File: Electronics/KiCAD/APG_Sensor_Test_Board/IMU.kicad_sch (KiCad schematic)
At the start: 6 parts, among them U2 BNO085

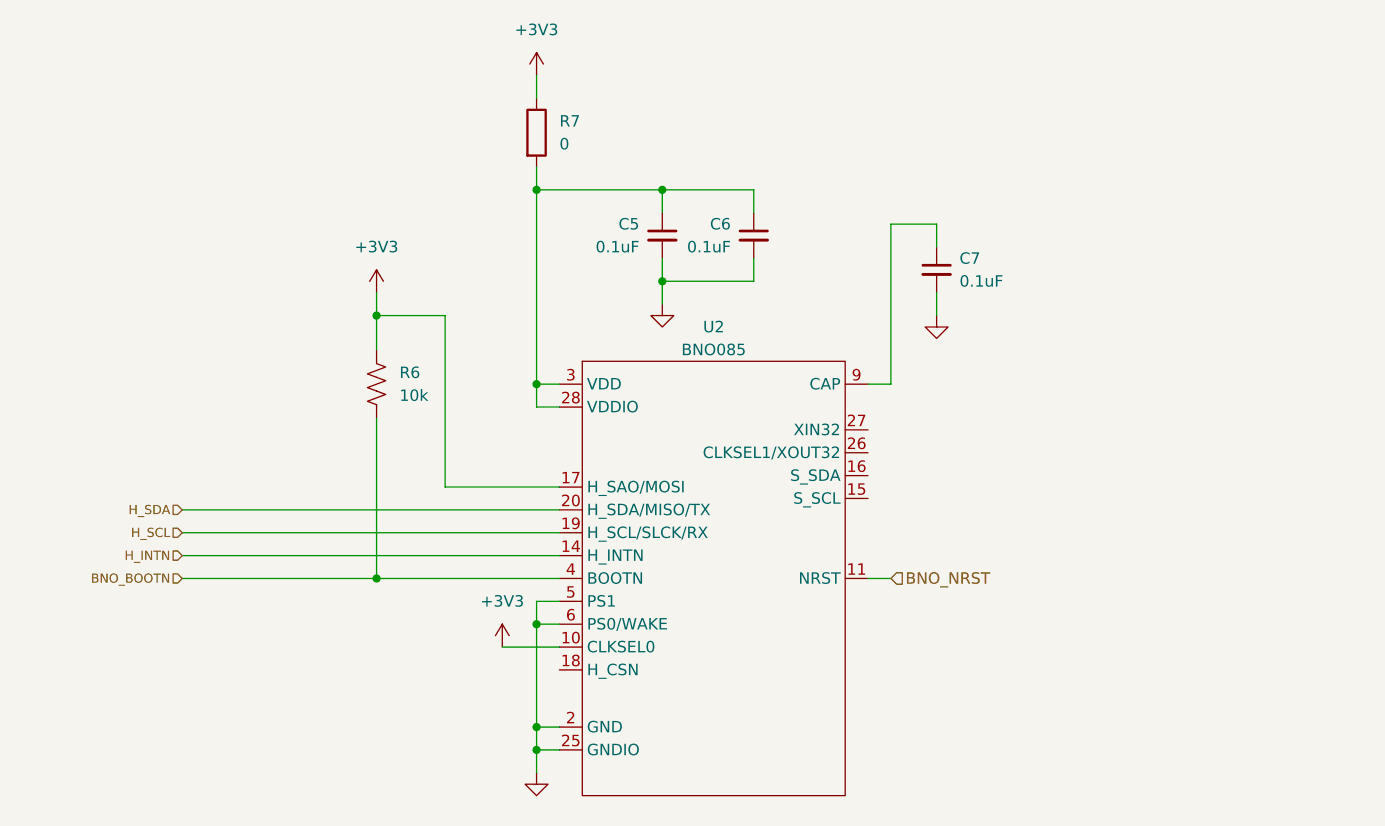
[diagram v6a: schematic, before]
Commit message: MOved IMU and HIGH G to SPI other misc changes
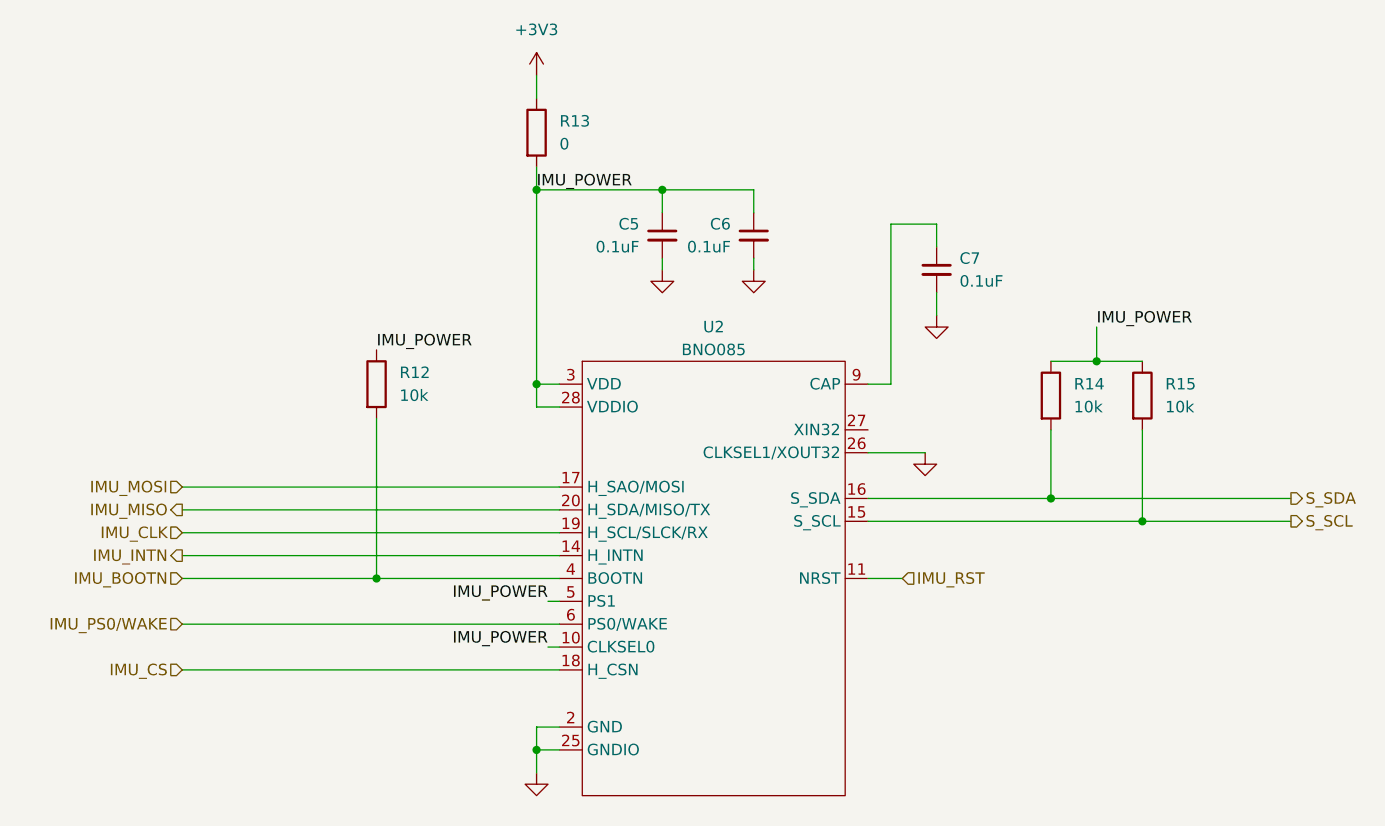
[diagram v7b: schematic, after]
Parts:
- removed R6: 10k, Resistor_SMD:R_0805_2012Metric, symbol Device:R_US
- added R12, R14, R15: 10k, Resistor_SMD:R_0805_2012Metric, symbol Device:R
- renumbered R7 to R13
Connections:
- net +3V3: no longer U2.10 (CLKSEL0), U2.17 (H_SAO/MOSI)
- net GND: now also U2.26 (CLKSEL1/XOUT32); no longer U2.5 (PS1), U2.6 (PS0/WAKE)
- net IMU_POWER: now reaches C5.1, C6.1, R13.2, U2.28 (VDDIO), U2.3 (VDD)
- net IMU_POWER: now also U2.10 (CLKSEL0), U2.5 (PS1), R12.1, R14.1, R15.1
- net S_SCL: now reaches U2.15 (S_SCL)
- net S_SCL: now also R15.2
- net S_SDA: now reaches U2.16 (S_SDA)
- net S_SDA: now also R14.2
- net IMU_CS: now reaches U2.18 (H_CSN)
- net BNO_BOOTN renamed IMU_BOOTN
- net IMU_BOOTN: now also R12.2
- net BNO_NRST renamed IMU_RST
- net H_INTN renamed IMU_INTN
- net H_SCL renamed IMU_CLK
- net H_SDA renamed IMU_MISO
- new net IMU_MOSI: U2.17 (H_SAO/MOSI)
- new net IMU_PS0/WAKE: U2.6 (PS0/WAKE)

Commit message: Layout and routing
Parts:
- added R29: 10k, Resistor_SMD:R_0603_1608Metric, symbol Device:R
- C5, C6, C7: footprint Capacitor_SMD:C_0805_2012Metric -> Capacitor_SMD:C_0603_1608Metric
- R12, R13, R14, R15: footprint Resistor_SMD:R_0805_2012Metric -> Resistor_SMD:R_0603_1608Metric
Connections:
- net IMU_CS: now also R29.2
- net IMU_POWER: now also R29.1
- net IMU_BOOTN: no longer names the net of R12.2, U2.4 (BOOTN)
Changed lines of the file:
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@@
+	)
+	(junction
+		(at 87.63 92.71)
+		(diameter 0)
+		(color 0 0 0 0)
 	)
 	(junction
@@
 	)
 	(junction
-		(at 102.87 82.55)
-		(diameter 0)
-		(color 0 0 0 0)
-	)
-	(junction
 		(at 134.62 39.37)
 		(diameter 0)
@@
 	(wire
 		(pts
+			(xy 87.63 64.77) (xy 87.63 92.71)
+		)
+		(stroke
+			(width 0)
+			(type default)
+		)
+	)
+	(wire
+		(pts
 			(xy 123.19 60.96) (xy 120.65 60.96)
 		)
@@
 	(wire
 		(pts
-			(xy 81.28 92.71) (xy 123.19 92.71)
+			(xy 81.28 92.71) (xy 87.63 92.71)
 		)
 		(stroke
@@
 	(wire
 		(pts
-			(xy 81.28 82.55) (xy 102.87 82.55)
+			(xy 87.63 92.71) (xy 123.19 92.71)
 		)
 		(stroke
@@
 	)
 	(label "IMU_POWER"
-		(at 121.92 90.17 180)
+		(at 87.63 57.15 0)
 		(fields_autoplaced yes)
 		(effects
@@
 				(size 1.27 1.27)
 			)
-			(justify right bottom)
+			(justify left bottom)
 		)
 	)
 	(label "IMU_POWER"
-		(at 121.92 85.09 180)
+		(at 121.92 90.17 180)
 		(fields_autoplaced yes)
 		(effects
@@
 	)
 	(label "IMU_POWER"
-		(at 102.87 57.15 0)
+		(at 121.92 85.09 180)
 		(fields_autoplaced yes)
 		(effects
@@
 				(size 1.27 1.27)
 			)
-			(justify left bottom)
+			(justify right bottom)
 		)
 	)
 	(label "IMU_POWER"
-		(at 120.65 39.37 0)
+		(at 102.87 57.15 0)
 		(fields_autoplaced yes)
 		(effects
@@
 		)
 	)
+	(label "IMU_POWER"
+		(at 120.65 39.37 0)
+		(fields_autoplaced yes)
+		(effects
+			(font
+				(size 1.27 1.27)
+			)
+			(justify left bottom)
+		)
+	)
 	(hierarchical_label "IMU_RST"
 		(shape input)
@@
 			)
 			(justify left)
-		)
-	)
-	(hierarchical_label "IMU_BOOTN"
-		(shape input)
-		(at 81.28 82.55 180)
-		(fields_autoplaced yes)
-		(effects
-			(font
-				(size 1.27 1.27)
-			)
-			(justify right)
 		)
 	)
@@
 			)
 		)
-		(property "Footprint" "Resistor_SMD:R_0805_2012Metric"
+		(property "Footprint" "Resistor_SMD:R_0603_1608Metric"
 			(at 118.872 33.02 90)
 			(effects
@@
 			)
 		)
-		(property "Footprint" "Resistor_SMD:R_0805_2012Metric"
+		(property "Footprint" "Resistor_SMD:R_0603_1608Metric"
 			(at 176.022 62.23 90)
 			(effects
@@
 			)
 		)
-		(property "Footprint" "Resistor_SMD:R_0805_2012Metric"
+		(property "Footprint" "Resistor_SMD:R_0603_1608Metric"
 			(at 101.092 60.96 90)
 			(effects
@@
 				(path "/3161be0c-372f-463d-be0a-bab00f344057/f8ef0a61-6d05-44d0-a94d-ca2583f2f5fd"
 					(reference "R12")
+					(unit 1)
+				)
+			)
+		)
+	)
+	(symbol
+		(lib_id "Device:R")
+		(at 87.63 60.96 0)
+		(unit 1)
+		(exclude_from_sim no)
+		(in_bom yes)
+		(on_board yes)
+		(dnp no)
+		(fields_autoplaced yes)
+		(property "Reference" "R29"
+			(at 90.17 59.6899 0)
+			(effects
+				(font
+					(size 1.27 1.27)
+				)
+				(justify left)
+			)
+		)
+		(property "Value" "10k"
+			(at 90.17 62.2299 0)
+			(effects
+				(font
+					(size 1.27 1.27)
+				)
+				(justify left)
+			)
+		)
+		(property "Footprint" "Resistor_SMD:R_0603_1608Metric"
+			(at 85.852 60.96 90)
+			(effects
+				(font
+					(size 1.27 1.27)
+				)
+				(hide yes)
+			)
+		)
+		(property "Datasheet" "~"
+			(at 87.63 60.96 0)
+			(effects
+				(font
+					(size 1.27 1.27)
+				)
+				(hide yes)
+			)
+		)
+		(property "Description" "Resistor"
+			(at 87.63 60.96 0)
+			(effects
+				(font
+					(size 1.27 1.27)
+				)
+				(hide yes)
+			)
+		)
+		(pin "2"
+		)
+		(pin "1"
+		)
+		(instances
+			(project "APG_Sensor_Test_Board"
+				(path "/3161be0c-372f-463d-be0a-bab00f344057/f8ef0a61-6d05-44d0-a94d-ca2583f2f5fd"
+					(reference "R29")
 					(unit 1)
 				)
@@
 			)
 		)
-		(property "Footprint" "Capacitor_SMD:C_0805_2012Metric"
+		(property "Footprint" "Capacitor_SMD:C_0603_1608Metric"
 			(at 144.78 44.45 0)
 			(effects
@@
 			)
 		)
-		(property "Footprint" "Capacitor_SMD:C_0805_2012Metric"
+		(property "Footprint" "Capacitor_SMD:C_0603_1608Metric"
 			(at 165.1 48.26 0)
 			(effects
@@
 			)
 		)
-		(property "Footprint" "Resistor_SMD:R_0805_2012Metric"
+		(property "Footprint" "Resistor_SMD:R_0603_1608Metric"
 			(at 186.182 62.23 90)
 			(effects
@@
 			)
 		)
-		(property "Footprint" "Capacitor_SMD:C_0805_2012Metric"
+		(property "Footprint" "Capacitor_SMD:C_0603_1608Metric"
 			(at 134.62 44.45 0)
 			(effects
